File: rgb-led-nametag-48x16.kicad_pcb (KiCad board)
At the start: 4 copper layers, 84 x 28.8 mm, 127 parts, among them J1 USB_C_Receptacle_USB2.0, J2 TagConnect_TC2030_SWD, Q1 CJ3139K, Q10 CJ3139K, Q11 CJ3139K, Q12 CJ3139K, Q13 CJ3139K, Q14 CJ3139K, Q15 CJ3139K, Q16 CJ3139K, Q2 CJ3139K, Q3 CJ3139K, Q4 CJ3139K, Q5 CJ3139K, Q6 CJ3139K, Q7 CJ3139K, Q8 CJ3139K, Q9 CJ3139K, U1 led-panel-16x16, U10 74HC595, U11 74HC595, U12 74HC595, U13 74HC595, U14 74HC595, U15 74HC595, U16 led-panel-16x16, U17 74HC595, U18 74HC595, U19 74HC595, U2 74HC595, U20 74HC595, U21 74HC595, U22 74HC595, U23 74HC595, U24 ESP32-PICO-D4, U25 STM32F722RETx, U26 SRV05-4, U27 TPS63001, U3 74HC595, U4 74HC595, U5 74HC595, U6 74HC595, U7 74HC595, U8 74HC595, U9 led-panel-16x16

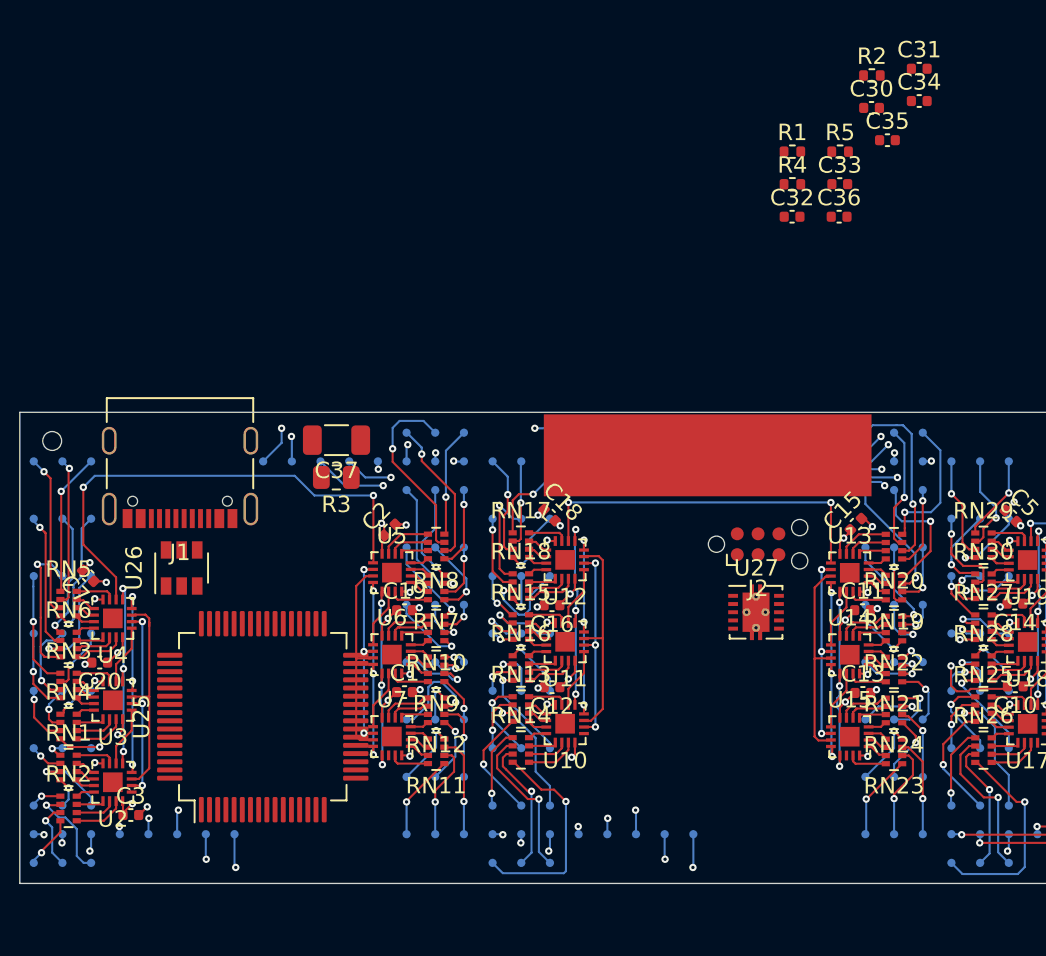
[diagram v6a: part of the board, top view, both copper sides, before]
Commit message: Make space for STM32
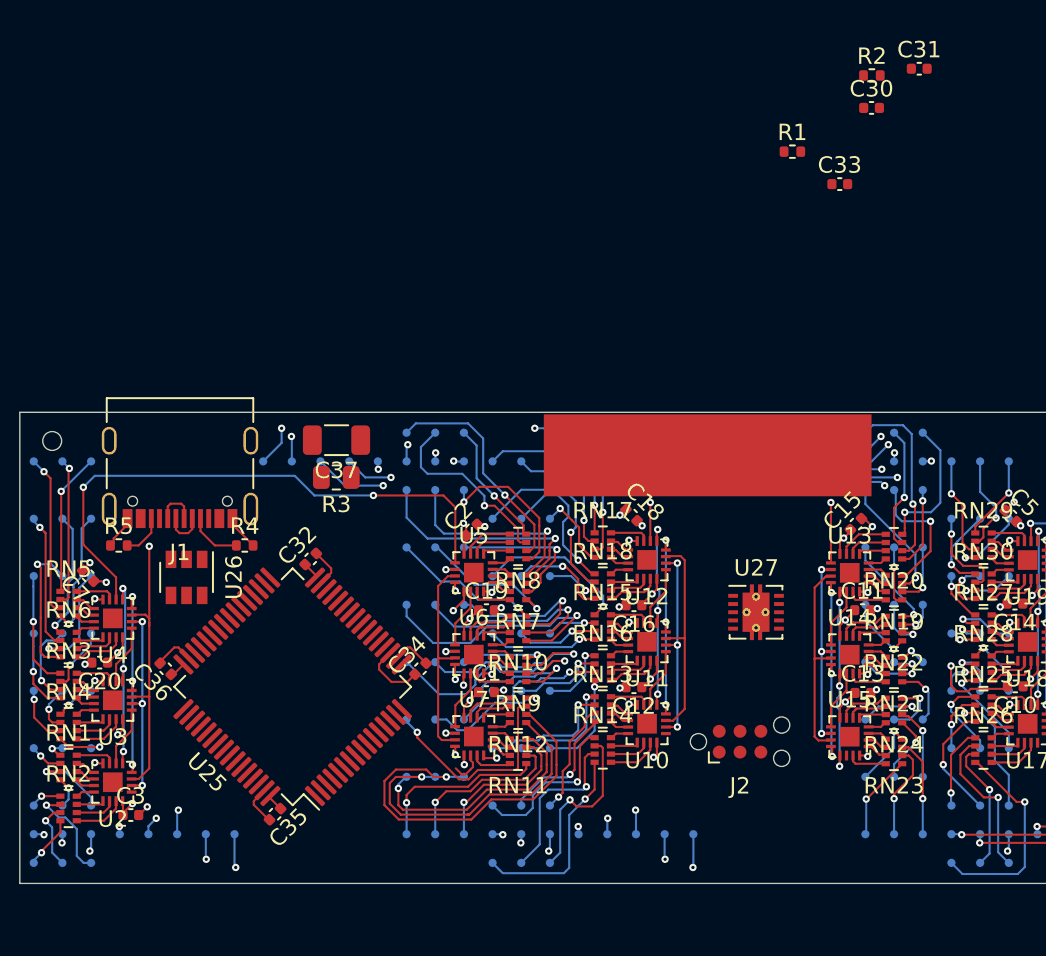
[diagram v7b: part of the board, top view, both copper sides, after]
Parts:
- moved C35 55.6 mm to (107.0, 119.2), turned to 225 degrees
- moved R5 50.1 mm to (97.5, 102.8)
- moved C36 49.5 mm to (100.3, 110.4), turned to 135 degrees
- moved C34 46.1 mm to (115.9, 110.4), turned to 45 degrees
- moved R4 40.0 mm to (105.2, 102.8)
- moved C32 36.0 mm to (109.2, 103.7), turned to 45 degrees
- moved J2 12.1 mm to (135.4, 114.8)
- moved C1 5.00 mm to (119.9, 111.8)
- moved C12 5.00 mm to (128.9, 111.5)
- moved C16 5.00 mm to (128.9, 106.5)
- moved C18 5.00 mm to (128.8, 101.0)
- moved C19 5.00 mm to (119.9, 106.8)
- moved C2 5.00 mm to (119.0, 101.9)
- moved RN10 5.00 mm to (121.8, 107.9)
- moved RN11 5.00 mm to (121.8, 115.4)
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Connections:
- U26 pad 1: Net-(U26-Pad1) -> /D-
- U26 pad 3: Net-(U26-Pad3) -> /D+
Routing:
- net /Panel 1/B4: track 4.79 -> 23.4 mm
- net /Panel 2/sheet61A6C351/SIN: track 22.1 -> 6.07 mm
- net /Panel 1/G4: track 4.18 -> 19.3 mm
- net GND: track 40.1 -> 54.3 mm
- net /Panel 1/R10: track 4.71 -> 16.2 mm
- net /Panel 1/R4: track 4.28 -> 14.8 mm
- net /Panel 1/G8: track 2.18 -> 12.6 mm
- net /Panel 1/R8: track 4.48 -> 14.4 mm
- net /Panel 1/G10: track 2.96 -> 12.5 mm
- net /Panel 1/B10: track 2.06 -> 9.88 mm
- net /Panel 2/R13: track 4.67 -> 11.8 mm
- net /Panel 1/R14: track 7.85 -> 14.9 mm
- net /Panel 1/R6: track 6.06 -> 13.1 mm
- net +3V3: track 0.00 -> 6.86 mm
- net /Panel 1/B6: track 2.80 -> 9.63 mm
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
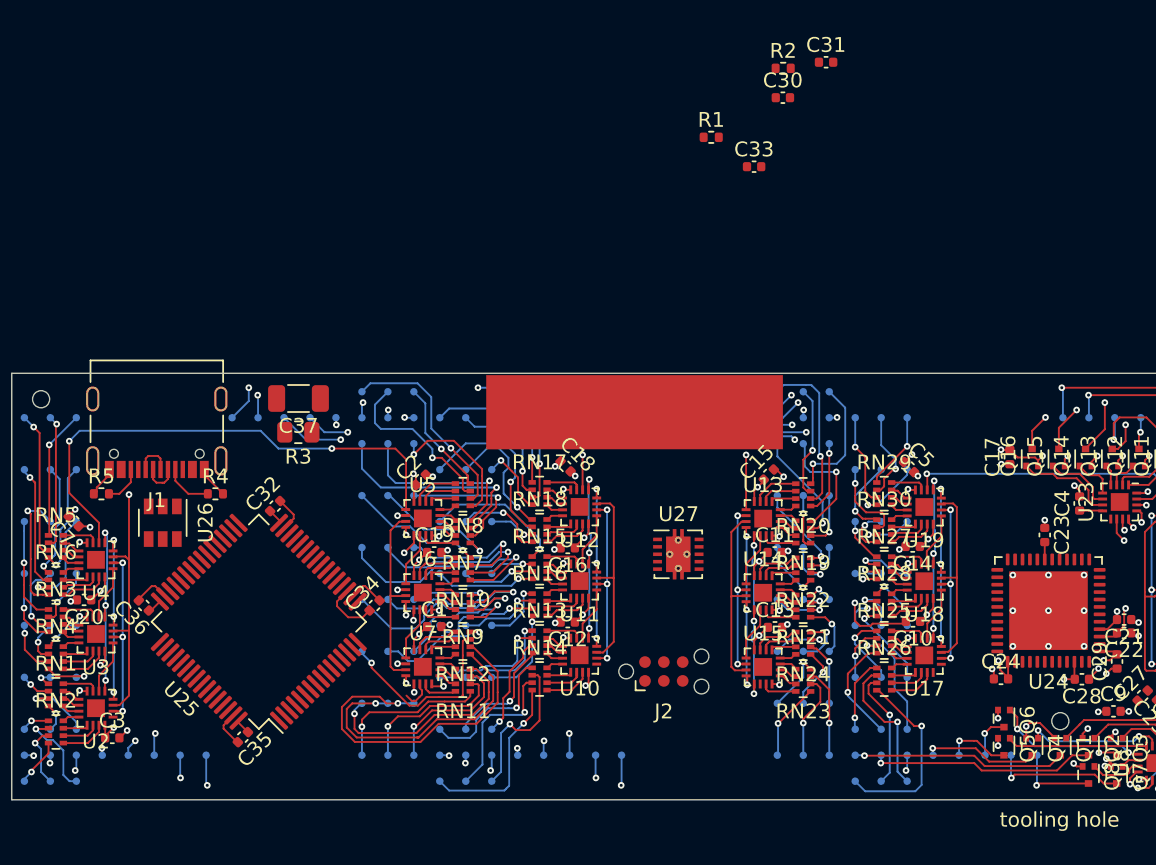
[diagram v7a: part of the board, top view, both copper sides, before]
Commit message: Route ESP32 SPI bus
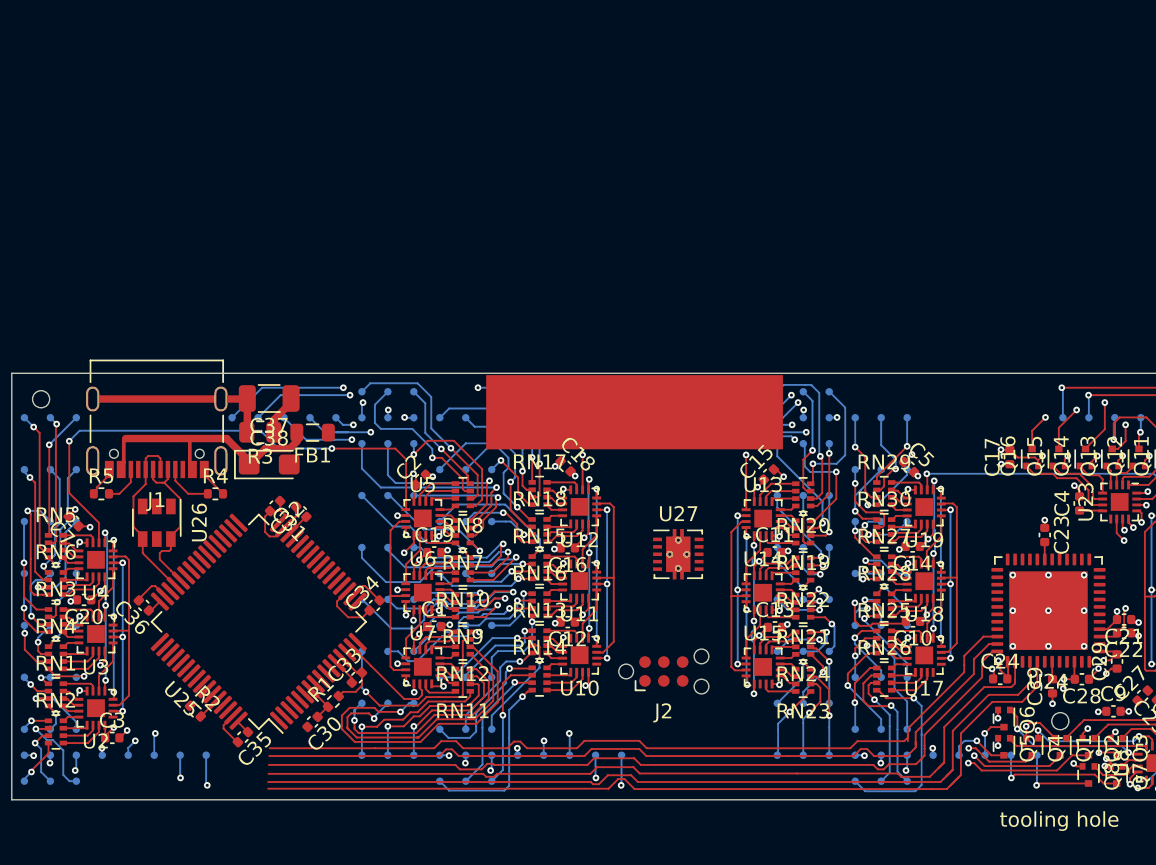
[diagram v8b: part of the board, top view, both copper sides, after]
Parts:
- added C38: 10uF, Capacitor_Tantalum_SMD:CP_EIA-3216-10_Kemet-I, F.Cu at (108.8, 100.9)
- added C39: 10uF, Capacitor_SMD:C_0402_1005Metric, F.Cu at (161.6, 115.8)
- added FB1: Bead, Inductor_SMD:L_0805_2012Metric, F.Cu at (111.7, 98.7)
- moved R2 58.7 mm to (103.8, 117.5), turned to 315 degrees
- moved C30 52.7 mm to (111.7, 118.2), turned to 225 degrees
- moved C31 46.6 mm to (110.9, 104.1), turned to 135 degrees
- moved R1 45.8 mm to (113.1, 116.8), turned to 45 degrees
- moved C33 43.6 mm to (114.7, 115.2), turned to 45 degrees
- moved R3 2.56 mm to (108.2, 98.7)
- moved C37 1.97 mm to (108.8, 96.4)
- moved U26 0.40 mm to (101.2, 104.8)
- turned C32 to 225 degrees
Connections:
- net /Sheet620161B9/VSPICLK renamed /Sheet620161B9/CLK
- net /Sheet620161B9/VSPICS renamed /Sheet620161B9/~CS
- net /Sheet620161B9/VSPID renamed /Sheet620161B9/MOSI
- net /Sheet620161B9/VSPIQ renamed /Sheet620161B9/MISO
- U22 pad 14: /QSPI_D3 -> /QSPI_D0
- U26 pad 1: /D- -> Net-(U26-Pad1)
- U26 pad 3: /D+ -> Net-(U26-Pad3)
- U26 pad 4: Net-(U26-Pad4) -> /D+
- U26 pad 6: Net-(U26-Pad6) -> /D-
- U7 pad 14: /QSPI_D0 -> /QSPI_D3
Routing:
- net /Sheet620161B9/TXD: track 0.00 -> 59.6 mm
- net /Sheet620161B9/RXD: track 0.00 -> 58.2 mm
- net /Sheet620161B9/MISO: track 0.00 -> 57.0 mm
- net /Sheet620161B9/~CS: track 0.00 -> 54.9 mm
- net /Sheet620161B9/CLK: track 0.00 -> 54.7 mm
- net /Sheet620161B9/MOSI: track 0.00 -> 54.6 mm
- net Net-(C38-Pad1): track 0.00 -> 17.9 mm
- net Net-(C37-Pad2): track 0.00 -> 12.8 mm
- net /D+: track 2.61 -> 12.0 mm
- net /D-: track 2.51 -> 11.0 mm
- net GND: track 54.3 -> 62.0 mm, vias 38 -> 39
- net /QSPI_D3: track 0.00 -> 7.06 mm
- net +3V3: track 6.86 -> 11.6 mm
- net /QSPI_CLK: track 81.1 -> 76.6 mm, vias 1 -> 0
- net /~RST: track 0.00 -> 2.75 mm
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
